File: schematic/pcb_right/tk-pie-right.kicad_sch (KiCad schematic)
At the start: 24 parts, among them J1 UART, J2 DBG

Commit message: Replicate left side update to right pcb
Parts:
- removed J1: UART, Connector_Audio:Jack_3.5mm_KoreanHropartsElec_PJ-320D-4A_Horizontal, symbol Connector_Audio:AudioJack4
- added MCU2: ~, KeyboardFootprints:DFR1075, symbol left_library:DFR1075
- added S12, S19: MX_SW_SOCKET_RGB_REV, Footprints:MX_SW_SOCKET_LED, symbol library:MX_SW_SOCKET_RGB
- added S18: ~, Footprints:MX_SW_SOCKET_LED_REV, symbol library:MX_SW_SOCKET_RGB_REV
- added S6: MX_SW_SOCKET_LED, Footprints:MX_SW_SOCKET_LED_REV, symbol library:MX_SW_SOCKET_RGB_REV
- renumbered S9 to S10, S10 to S11, S11 to S13, S12 to S14, S13 to S15, S14 to S16, S15 to S17, S6 to S7, S7 to S8, S8 to S9
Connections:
- net +5V: now also S19.4 (5V)
- net GND: now also MCU2.GND (Ground), S12.2 (R), S18.2 (R), S19.2 (R), S19.3 (G), S6.2 (R)
- net S10: now also S10.1 (L); no longer S11.1 (L)
- net S11: now also S11.1 (L); no longer S13.1 (L)
- net S12: now also S12.1 (L); no longer S14.1 (L)
- net S13: now also S13.1 (L); no longer S15.1 (L)
- net S14: now also S14.1 (L); no longer S16.1 (L)
- net S15: now also S15.1 (L); no longer S17.1 (L)
- net S16: now also S16.1 (L); no longer E4.1 (Pin_1)
- net S17: now also S17.1 (L); no longer E5.1 (Pin_1)
- net S18: now also S18.1 (L); no longer E6.1 (Pin_1)
- net S6: now also S6.1 (L); no longer S7.1 (L)
- net S7: now also S7.1 (L); no longer S8.1 (L)
- net S8: now also S8.1 (L), MCU2.1 (D1), MCU2.14 (D14), MCU2.15 (D15), MCU2.16 (TX), MCU2.17 (RX), MCU2.18 (CMD), MCU2.19 (SDA), MCU2.2 (D2), MCU2.20 (SCL), MCU2.21 (DAT1), MCU2.22 (DAT2), MCU2.23 (DAT3), MCU2.3 (D3), MCU2.4 (LP_RX), MCU2.5 (LP_TX), MCU2.6 (D6), MCU2.7 (D7), MCU2.8 (D8), MCU2.9 (D9); no longer S9.1 (L)
- net S9: now also S9.1 (L); no longer S10.1 (L)
- net at E3.1 (Pin_1): now also S19.6 (DOUT); no longer S17.6 (DOUT)
- net at S5.6 (DOUT): now also S6.5 (DIN); no longer S11.5 (DIN)
- new net: S12.5 (DIN), S6.6 (DOUT)
- new net: S17.6 (DOUT), S18.5 (DIN)
- new net: S18.6 (DOUT), S19.5 (DIN)
- new net: S11.5 (DIN), S12.6 (DOUT)
- new net +3.3V: MCU2.3V3 (3.3V)
- new net S19: S19.1 (L)
- new net S20: E4.1 (Pin_1)
- new net S21: E5.1 (Pin_1)
- new net S22: E6.1 (Pin_1)
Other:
- moved on the sheet: E1, E2, E3, E4, E5, E6, J2, MCU1, S13, S14, S15, S16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

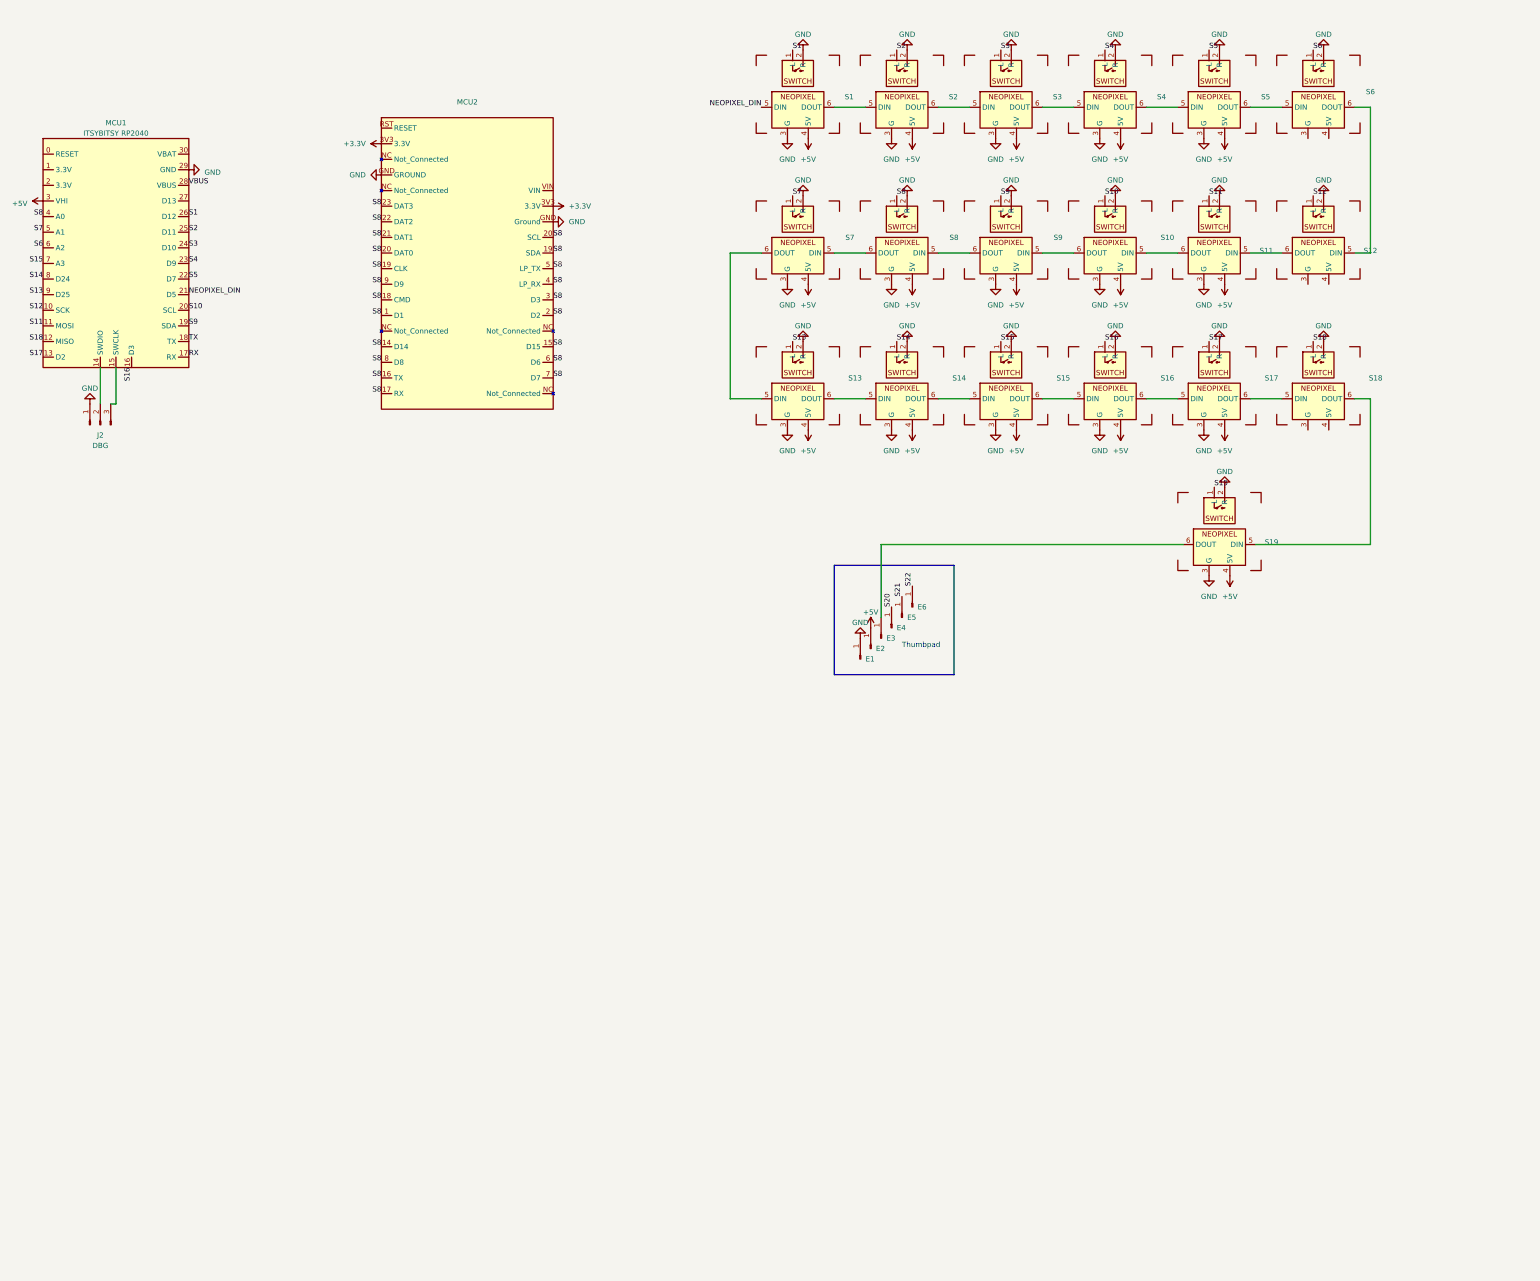
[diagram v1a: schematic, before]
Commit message: Copy tk-pie-left to right and auto-flip it
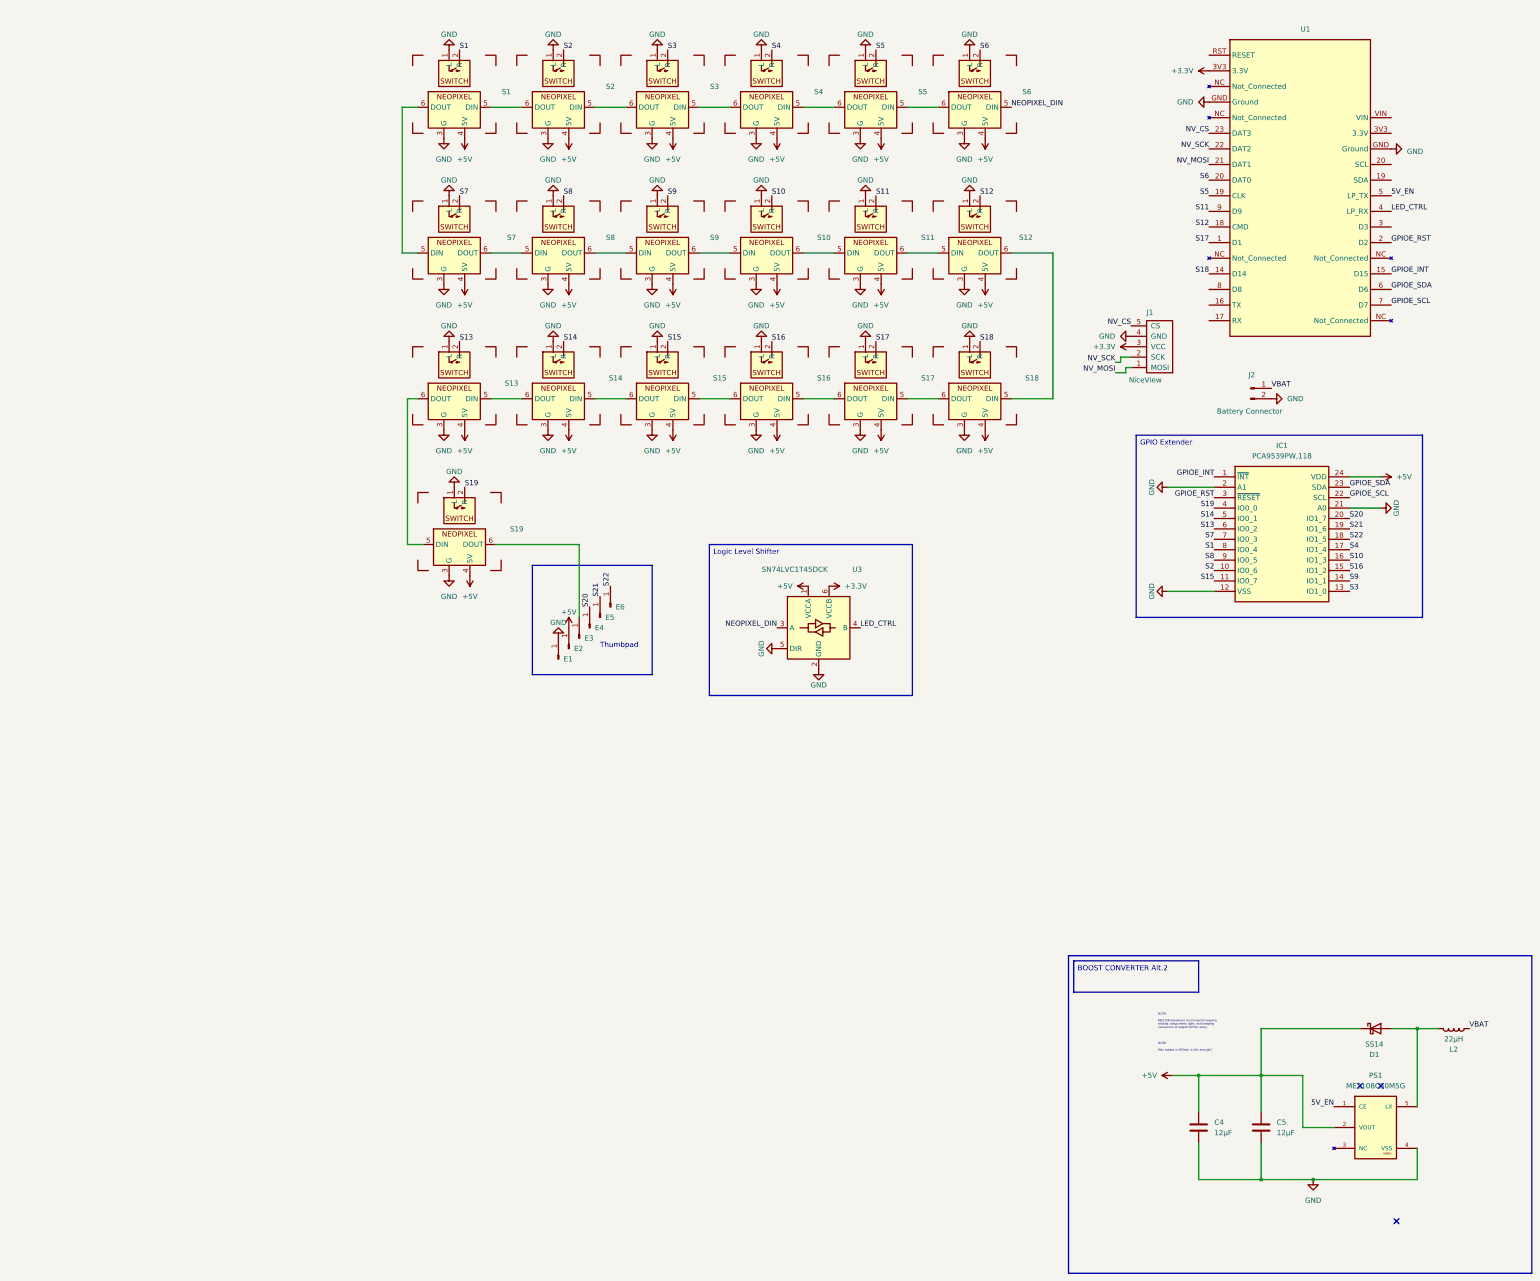
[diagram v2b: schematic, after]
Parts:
- removed J2: DBG, Connector_PinSocket_2.54mm:PinSocket_1x03_P2.54mm_Vertical, symbol Connector:Conn_01x03_Pin
- removed MCU1: ITSYBITSY RP2040, Footprints:ITSYBITSY BREAKOUT, symbol library:ITSYBITSY_RP2040
- removed MCU2: ~, KeyboardFootprints:DFR1075, symbol left_library:DFR1075
- removed S12, S19: MX_SW_SOCKET_RGB_REV, Footprints:MX_SW_SOCKET_LED, symbol library:MX_SW_SOCKET_RGB
- removed S18: ~, Footprints:MX_SW_SOCKET_LED_REV, symbol library:MX_SW_SOCKET_RGB_REV
- removed S6: MX_SW_SOCKET_LED, Footprints:MX_SW_SOCKET_LED_REV, symbol library:MX_SW_SOCKET_RGB_REV
- added C4, C5: 12µF, Capacitor_SMD:C_1210_3225Metric_Pad1.33x2.70mm_HandSolder, symbol Device:C
- added D1: SS14, Diode_SMD:D_SMA, symbol Diode:SS14
- added IC1: PCA9539PW,118, SOP65P640X110-24N, symbol library:PCA9539PW,118
- added J1: NiceView, Footprints:Nice!View Header, symbol library:NiceView Header
- added J2: Battery Connector, Connector_JST:JST_PH_S2B-PH-SM4-TB_1x02-1MP_P2.00mm_Horizontal, symbol Connector:Conn_01x02_Pin
- added L2: 22µH, Inductor_SMD:L_Cenker_CKCS5040, symbol Device:L
- added PS1: ME2108C50M5G, Package_TO_SOT_SMD:SOT-23-5, symbol library:ME2108C50M5G
- added S1, S13: MX_SW_SOCKET_LED, Footprints:MX_SW_SOCKET_LED, symbol library:MX_SW_SOCKET_RGB
- added S19, S7: MX_SW_SOCKET_RGB_REV, Footprints:MX_SW_SOCKET_LED_REV, symbol library:MX_SW_SOCKET_RGB_REV
- added U1: ~, Footprints:DFR1075, symbol library:DFR1075
- added U3: SN74LVC1T45DCK, Package_TO_SOT_SMD:SOT-363_SC-70-6_Handsoldering, symbol Logic_LevelTranslator:SN74LVC1T45DCK
- S10: renamed from S9; footprint Footprints:MX_SW_SOCKET_LED -> Footprints:MX_SW_SOCKET_LED_REV; symbol library:MX_SW_SOCKET_RGB -> library:MX_SW_SOCKET_RGB_REV
- S11: renamed from S10; footprint Footprints:MX_SW_SOCKET_LED -> Footprints:MX_SW_SOCKET_LED_REV; symbol library:MX_SW_SOCKET_RGB -> library:MX_SW_SOCKET_RGB_REV
- S12: renamed from S11; footprint Footprints:MX_SW_SOCKET_LED -> Footprints:MX_SW_SOCKET_LED_REV; symbol library:MX_SW_SOCKET_RGB -> library:MX_SW_SOCKET_RGB_REV
- S14: renamed from S13; footprint Footprints:MX_SW_SOCKET_LED_REV -> Footprints:MX_SW_SOCKET_LED; symbol library:MX_SW_SOCKET_RGB_REV -> library:MX_SW_SOCKET_RGB
- S15: renamed from S14; footprint Footprints:MX_SW_SOCKET_LED_REV -> Footprints:MX_SW_SOCKET_LED; symbol library:MX_SW_SOCKET_RGB_REV -> library:MX_SW_SOCKET_RGB
- S16: renamed from S15; footprint Footprints:MX_SW_SOCKET_LED_REV -> Footprints:MX_SW_SOCKET_LED; symbol library:MX_SW_SOCKET_RGB_REV -> library:MX_SW_SOCKET_RGB
- S17: renamed from S16; footprint Footprints:MX_SW_SOCKET_LED_REV -> Footprints:MX_SW_SOCKET_LED; symbol library:MX_SW_SOCKET_RGB_REV -> library:MX_SW_SOCKET_RGB
- S18: renamed from S17; footprint Footprints:MX_SW_SOCKET_LED_REV -> Footprints:MX_SW_SOCKET_LED; symbol library:MX_SW_SOCKET_RGB_REV -> library:MX_SW_SOCKET_RGB
- S2: renamed from S1; footprint Footprints:MX_SW_SOCKET_LED_REV -> Footprints:MX_SW_SOCKET_LED; symbol library:MX_SW_SOCKET_RGB_REV -> library:MX_SW_SOCKET_RGB
- S3: renamed from S2; footprint Footprints:MX_SW_SOCKET_LED_REV -> Footprints:MX_SW_SOCKET_LED; symbol library:MX_SW_SOCKET_RGB_REV -> library:MX_SW_SOCKET_RGB
- S4: renamed from S3; footprint Footprints:MX_SW_SOCKET_LED_REV -> Footprints:MX_SW_SOCKET_LED; symbol library:MX_SW_SOCKET_RGB_REV -> library:MX_SW_SOCKET_RGB
- S5: renamed from S4; footprint Footprints:MX_SW_SOCKET_LED_REV -> Footprints:MX_SW_SOCKET_LED; symbol library:MX_SW_SOCKET_RGB_REV -> library:MX_SW_SOCKET_RGB
- S6: renamed from S5; footprint Footprints:MX_SW_SOCKET_LED_REV -> Footprints:MX_SW_SOCKET_LED; symbol library:MX_SW_SOCKET_RGB_REV -> library:MX_SW_SOCKET_RGB
- S8: renamed from S7; footprint Footprints:MX_SW_SOCKET_LED -> Footprints:MX_SW_SOCKET_LED_REV; symbol library:MX_SW_SOCKET_RGB -> library:MX_SW_SOCKET_RGB_REV
- S9: renamed from S8; footprint Footprints:MX_SW_SOCKET_LED -> Footprints:MX_SW_SOCKET_LED_REV; symbol library:MX_SW_SOCKET_RGB -> library:MX_SW_SOCKET_RGB_REV
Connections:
- net +3.3V: now also J1.3 (VCC), U1.3V3 (3.3V), U3.6 (VCCB)
- net +5V: now also C4.1, C5.2, D1.1 (K), IC1.24 (VDD), PS1.2 (VOUT), S1.4 (5V), S13.4 (5V), S19.4 (5V), S7.4 (5V), U3.1 (VCCA)
- net GND: now also S10.1 (L), S11.1 (L), S12.1 (L), S14.1 (L), S15.1 (L), S16.1 (L), S17.1 (L), S18.1 (L), S2.1 (L), S3.1 (L), S4.1 (L), S5.1 (L), S6.1 (L), S8.1 (L), S9.1 (L), C4.2, C5.1, IC1.12 (VSS), IC1.2 (A1), IC1.21 (A0), J1.4 (GND), J2.2 (Pin_2), PS1.4 (VSS), S1.1 (L), S1.3 (G), S13.1 (L), S13.3 (G), S19.1 (L), S19.3 (G), S7.1 (L), S7.3 (G), U1.GND (Ground), U3.2 (GND), U3.5 (DIR); no longer S10.2 (R), S11.2 (R), S12.2 (R), S14.2 (R), S15.2 (R), S16.2 (R), S17.2 (R), S18.2 (R), S2.2 (R), S3.2 (R), S4.2 (R), S5.2 (R), S6.2 (R), S8.2 (R), S9.2 (R)
- net NEOPIXEL_DIN: now also S6.5 (DIN), U3.3 (A); no longer S2.5 (DIN)
- net S1: now also IC1.8 (IO0_4), S1.2 (R); no longer S2.1 (L)
- net S10: now also S10.2 (R), IC1.16 (IO1_3); no longer S11.1 (L)
- net S11: now also S11.2 (R), U1.9 (D9); no longer S12.1 (L)
- net S12: now also S12.2 (R), U1.18 (CMD)
- net S13: now also IC1.6 (IO0_2), S13.2 (R); no longer S14.1 (L)
- net S14: now also S14.2 (R), IC1.5 (IO0_1); no longer S15.1 (L)
- net S15: now also S15.2 (R), IC1.11 (IO0_7); no longer S16.1 (L)
- net S16: now also S16.2 (R), IC1.15 (IO1_2); no longer S17.1 (L)
- net S17: now also S17.2 (R), U1.1 (D1); no longer S18.1 (L)
- net S18: now also S18.2 (R), U1.14 (D14)
- net S19: now also IC1.4 (IO0_0), S19.2 (R)
- net S2: now also S2.2 (R), IC1.10 (IO0_6); no longer S3.1 (L)
- net S20: now also IC1.20 (IO1_7)
- net S21: now also IC1.19 (IO1_6)
- net S22: now also IC1.18 (IO1_5)
- net S3: now also S3.2 (R), IC1.13 (IO1_0); no longer S4.1 (L)
- net S4: now also S4.2 (R), IC1.17 (IO1_4); no longer S5.1 (L)
- net S5: now also S5.2 (R), U1.19 (SDA); no longer S6.1 (L)
- net S6: now also S6.2 (R), U1.20 (SCL)
- net S7: now also IC1.7 (IO0_3), S7.2 (R); no longer S8.1 (L)
- net S8: now also S8.2 (R), IC1.9 (IO0_5); no longer S9.1 (L)
- net S9: now also S9.2 (R), IC1.14 (IO1_1); no longer S10.1 (L)
- net at S5.5 (DIN): now also S6.6 (DOUT); no longer S4.6 (DOUT)
- net at S5.6 (DOUT): now also S4.5 (DIN); no longer S6.5 (DIN)
- net at S8.5 (DIN): now also S7.6 (DOUT); no longer S9.6 (DOUT)
- net at S8.6 (DOUT): now also S9.5 (DIN); no longer S14.5 (DIN)
- net at S17.5 (DIN): now also S18.6 (DOUT); no longer S16.6 (DOUT)
- net at S17.6 (DOUT): now also S16.5 (DIN); no longer S18.5 (DIN)
- net at E3.1 (Pin_1): now also S19.6 (DOUT)
- net at S15.5 (DIN): now also S16.6 (DOUT); no longer S14.6 (DOUT)
- net at S15.6 (DOUT): now also S14.5 (DIN); no longer S16.5 (DIN)
- net at S2.6 (DOUT): now also S1.5 (DIN); no longer S3.5 (DIN)
- net at S11.5 (DIN): now also S10.6 (DOUT); no longer S12.6 (DOUT)
- net at S11.6 (DOUT): now also S12.5 (DIN); no longer S10.5 (DIN)
- net at S3.6 (DOUT): now also S2.5 (DIN); no longer S4.5 (DIN)
- new net: S1.6 (DOUT), S7.5 (DIN)
- new net: D1.2 (A), L2.2, PS1.5 (LX)
- new net: S13.6 (DOUT), S19.5 (DIN)
- new net: S10.5 (DIN), S9.6 (DOUT)
- new net: S13.5 (DIN), S14.6 (DOUT)
- new net: S12.6 (DOUT), S18.5 (DIN)
- new net: S3.5 (DIN), S4.6 (DOUT)
- new net  NV_CS: J1.5 (CS), U1.23 (DAT3)
- new net 5V_EN: PS1.1 (CE), U1.5 (LP_TX)
- new net GPIOE_INT: IC1.1 (~{INT}), U1.15 (D15)
- new net GPIOE_RST: IC1.3 (~{RESET}), U1.2 (D2)
- new net GPIOE_SCL: IC1.22 (SCL), U1.7 (D7)
- new net GPIOE_SDA: IC1.23 (SDA), U1.6 (D6)
- new net LED_CTRL: U1.4 (LP_RX), U3.4 (B)
- new net NV_MOSI: J1.1 (MOSI), U1.21 (DAT1)
- new net NV_SCK: J1.2 (SCK), U1.22 (DAT2)
- new net VBAT: J2.1 (Pin_1), L2.1
- no-connect marks 0 -> 3
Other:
- note added: "NOTE: ME2108 datasheet recommends keeping related components tight, and keeping consumers of output further away."
- note added: "NOTE: Max output is 400mA. is this enough?"
- moved on the sheet: E1, E2, E3, E4, E5, E6, S10, S11, S12, S14, S15, S16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

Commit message: RIGHT PCB ???? TRACES VIAS!!!!
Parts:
- S1, S13, S4, S5, S6: value MX_SW_SOCKET_LED -> MX_SW_SOCKET_RGB_REV; footprint Footprints:MX_SW_SOCKET_LED -> Footprints:MX_SW_SOCKET_LED_REV; symbol library:MX_SW_SOCKET_RGB -> library:MX_SW_SOCKET_RGB_REV
- S10, S11, S12, S19, S7, S8, S9: value MX_SW_SOCKET_RGB_REV -> MX_SW_SOCKET_LED; footprint Footprints:MX_SW_SOCKET_LED_REV -> Footprints:MX_SW_SOCKET_LED; symbol library:MX_SW_SOCKET_RGB_REV -> library:MX_SW_SOCKET_RGB
- S14, S15, S16, S17, S18, S2, S3: value ~ -> MX_SW_SOCKET_RGB_REV; footprint Footprints:MX_SW_SOCKET_LED -> Footprints:MX_SW_SOCKET_LED_REV; symbol library:MX_SW_SOCKET_RGB -> library:MX_SW_SOCKET_RGB_REV
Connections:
- net +3.3V: now also IC1.24 (VDD)
- net +5V: no longer IC1.24 (VDD)
- net GND: now also S1.2 (R), S10.2 (R), S11.2 (R), S12.2 (R), S13.2 (R), S14.2 (R), S15.2 (R), S16.2 (R), S17.2 (R), S18.2 (R), S19.2 (R), S2.2 (R), S3.2 (R), S4.2 (R), S5.2 (R), S6.2 (R), S7.2 (R), S8.2 (R), S9.2 (R); no longer S1.1 (L), S10.1 (L), S11.1 (L), S12.1 (L), S13.1 (L), S14.1 (L), S15.1 (L), S16.1 (L), S17.1 (L), S18.1 (L), S19.1 (L), S2.1 (L), S3.1 (L), S4.1 (L), S5.1 (L), S6.1 (L), S7.1 (L), S8.1 (L), S9.1 (L)
- net S1: now also IC1.6 (IO0_2), S1.1 (L); no longer IC1.8 (IO0_4), S1.2 (R)
- net S10: now also IC1.17 (IO1_4), S10.1 (L); no longer IC1.16 (IO1_3), S10.2 (R)
- net S11: now also S11.1 (L); no longer S11.2 (R)
- net S12: now also S12.1 (L); no longer S12.2 (R)
- net S13: now also IC1.9 (IO0_5), S13.1 (L); no longer IC1.6 (IO0_2), S13.2 (R)
- net S14: now also IC1.10 (IO0_6), S14.1 (L); no longer IC1.5 (IO0_1), S14.2 (R)
- net S15: now also IC1.4 (IO0_0), S15.1 (L); no longer IC1.11 (IO0_7), S15.2 (R)
- net S16: now also IC1.18 (IO1_5), S16.1 (L); no longer IC1.15 (IO1_2), S16.2 (R)
- net S17: now also S17.1 (L); no longer S17.2 (R)
- net S18: now also S18.1 (L); no longer S18.2 (R)
- net S19: now also IC1.11 (IO0_7), S19.1 (L); no longer IC1.4 (IO0_0), S19.2 (R)
- net S2: now also IC1.5 (IO0_1), S2.1 (L); no longer IC1.10 (IO0_6), S2.2 (R)
- net S20: now also IC1.13 (IO1_0); no longer IC1.20 (IO1_7)
- net S21: now also IC1.14 (IO1_1); no longer IC1.19 (IO1_6)
- net S22: now also IC1.15 (IO1_2); no longer IC1.18 (IO1_5)
- net S3: now also IC1.20 (IO1_7), S3.1 (L); no longer IC1.13 (IO1_0), S3.2 (R)
- net S4: now also IC1.16 (IO1_3), S4.1 (L); no longer IC1.17 (IO1_4), S4.2 (R)
- net S5: now also S5.1 (L); no longer S5.2 (R)
- net S6: now also S6.1 (L); no longer S6.2 (R)
- net S7: now also IC1.8 (IO0_4), S7.1 (L); no longer IC1.7 (IO0_3), S7.2 (R)
- net S8: now also IC1.7 (IO0_3), S8.1 (L); no longer IC1.9 (IO0_5), S8.2 (R)
- net S9: now also IC1.19 (IO1_6), S9.1 (L); no longer IC1.14 (IO1_1), S9.2 (R)
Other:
- moved on the sheet: E1, E2, E3, E4, E5, E6, IC1, J1, J2, S1, S10, S11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

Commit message: Save Ferris
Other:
- moved on the sheet: IC1
